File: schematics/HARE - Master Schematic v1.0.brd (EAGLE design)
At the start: 105.1 x 80 mm, 97 parts, among them IC1 NE5532N, IC2 NE5532N, IC3 FT232RL, IC4 NE5532N, IC5 7805DT, IC6 AT25P, J1 9V, J2 STEREOSW, J3 STEREOSW, Q1 16 MHz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

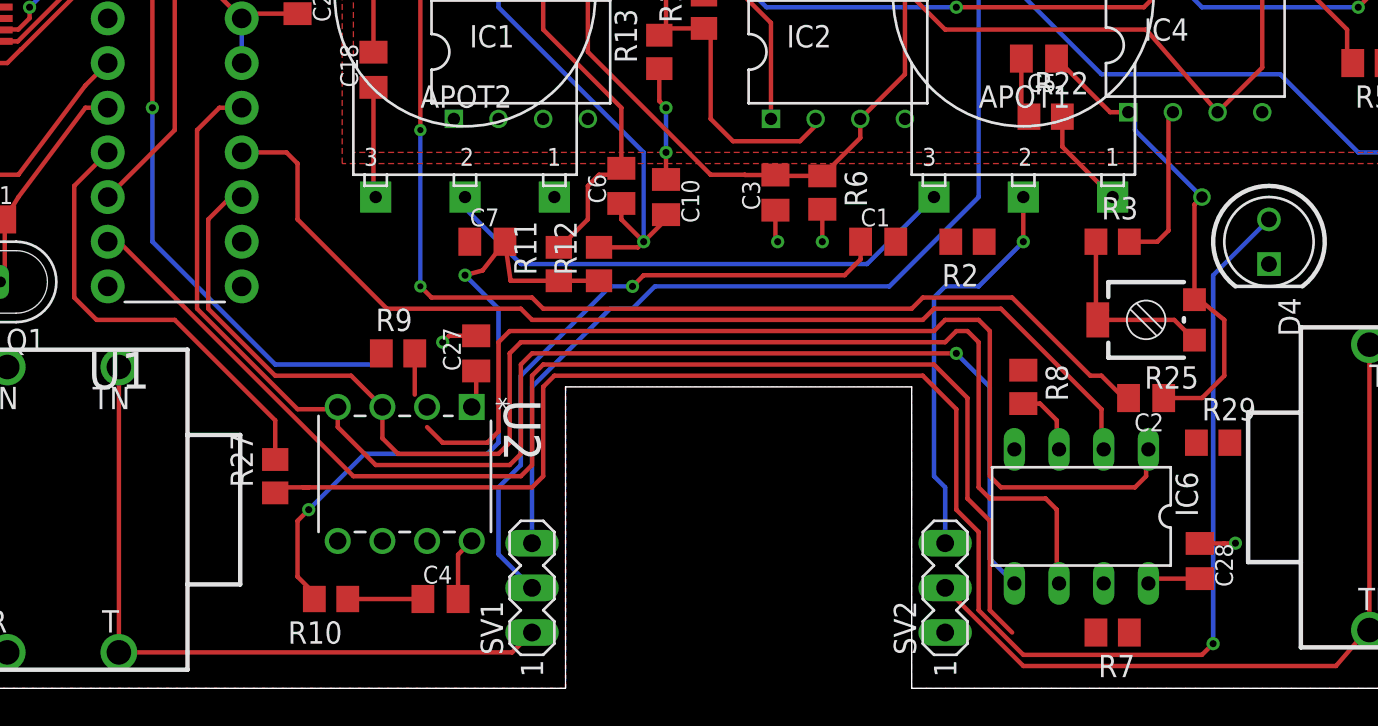
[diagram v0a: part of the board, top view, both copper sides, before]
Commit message: no DRC errors in board file
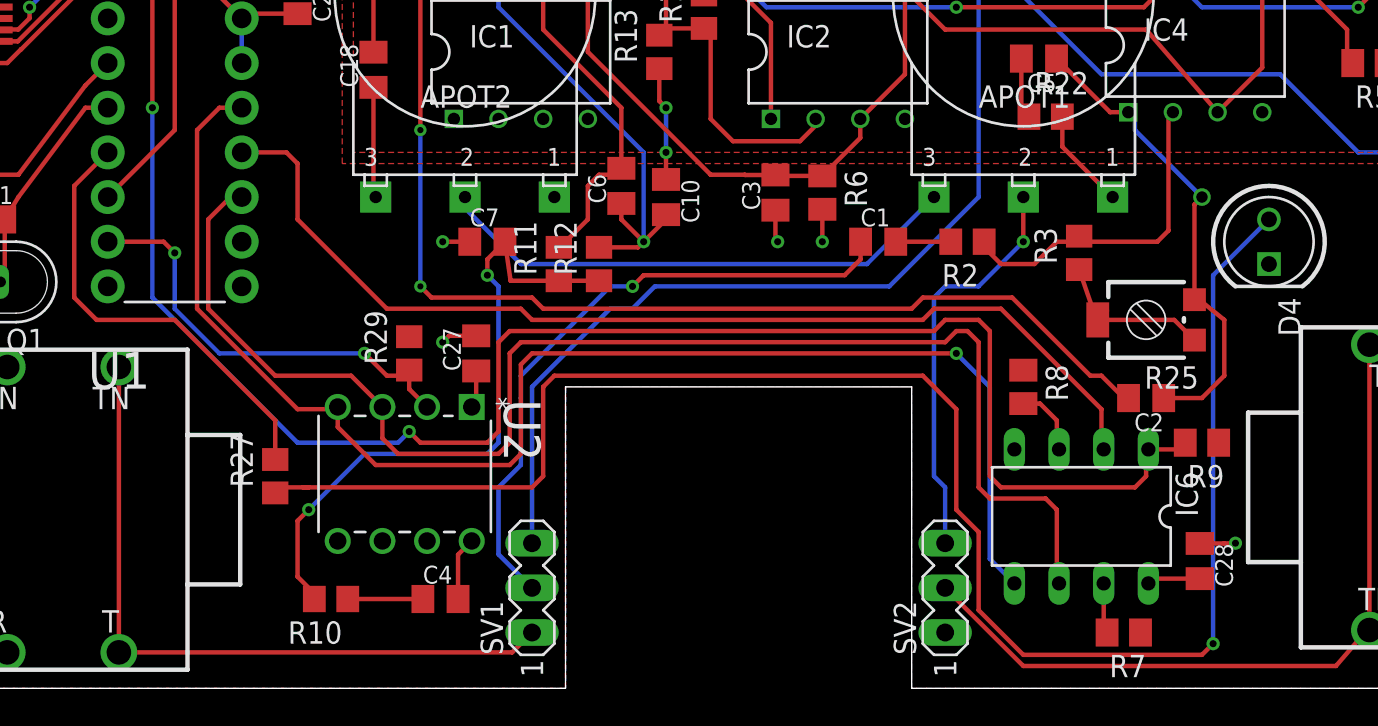
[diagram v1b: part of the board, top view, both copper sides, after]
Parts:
- moved R29 46.0 mm to (33.7, 19.1), turned to 90 degrees
- moved R9 46.0 mm to (78.7, 14.0), turned to 180 degrees
- moved R3 2.01 mm to (71.8, 24.8), turned to 90 degrees
- moved R7 0.64 mm to (74.3, 3.17)
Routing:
- net DAC_CS: track 75.2 -> 25.4 mm, vias 0 -> 2
- net N$11: track 9.32 -> 19.1 mm
- net MEM_CS: track 95.8 -> 102.0 mm, vias 1 -> 2
- net N$10: track 0.00 -> 3.13 mm
- net N$8: track 0.00 -> 2.83 mm
- net GND: track 62.4 -> 63.9 mm, vias 24 -> 25
- net N$49: track 11.4 -> 9.99 mm
- net N$16: track 38.8 -> 37.5 mm

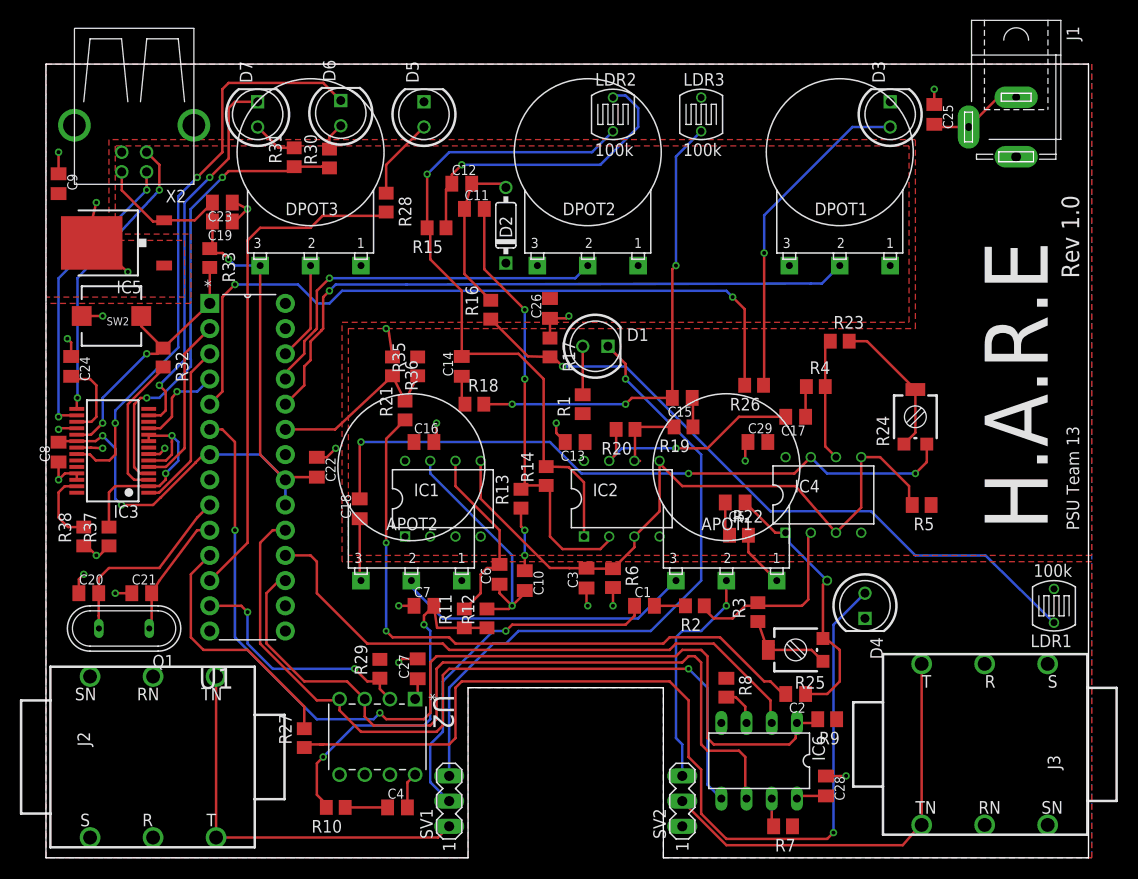
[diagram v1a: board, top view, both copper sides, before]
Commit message: PWM-to-DC converter added for VCA control, VCF changes fixed, and fuse added
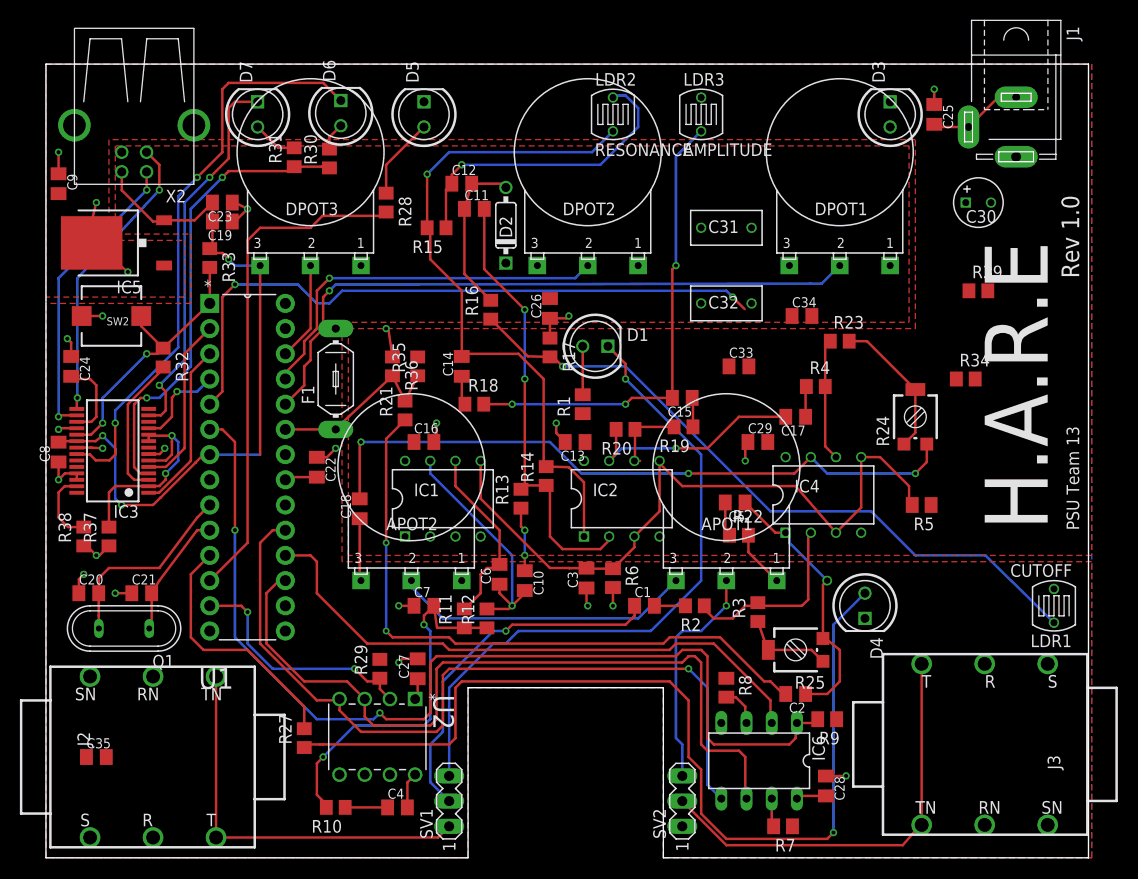
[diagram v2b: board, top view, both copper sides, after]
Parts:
- removed R26: 1k, resistor:R0805
- added C30: 22uF, gm-caps-electro-pol:050_020_1
- added C31, C32: 470nF, gm-caps-film-box:072X035
- added C33, C34: 0.1uF, resistor:C0805K
- added C35: .1uF, resistor:C0805K
- added F1: FUSELITTLEFUSE, fuse:LITTLEFUSE
- added R34, R39: 1k, resistor:R0805
- D3: value LED5MM -> AMPLITUDE
- D4: value LED5MM -> CUTOFF
- D5: value LED5MM -> RESONANCE
- LDR1: value 100k -> CUTOFF
- LDR2: value 100k -> RESONANCE
- LDR3: value 100k -> AMPLITUDE
- R27: value 2.2k -> 1k
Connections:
- removed net N$60: R26.2, U1.5
- removed net N$61: D3.A, R26.1
- new net +5V1: C33.2, U1.21
- new net N$15: C30.+, IC1.2, R34.2, R39.1
- new net N$19: D3.A, IC1.1, R39.2
- new net N$34: C9.2, F1.2, IC5.1
- new net PWM_DC: R34.1, U1.5
- net +5V: now also C16.1, C34.2, IC1.8; no longer U1.21
- net GND: now also C30.-, C31.2, C32.2, C33.1, C34.1, C35.1
- net N$57: now also C31.1
- net N$59: now also C32.1
- net VCC: now also F1.1; no longer C16.1, C9.2, IC1.8, IC5.1
- net V_BIAS: now also C35.2, IC1.3
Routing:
- net N$60: track 74.3 -> 0.00 mm, vias 2 -> 0
- net PWM_DC: track 0.00 -> 66.6 mm, vias 0 -> 2
- net N$61: track 33.6 -> 0.00 mm, vias 1 -> 0
- net +5V: track 89.4 -> 79.3 mm

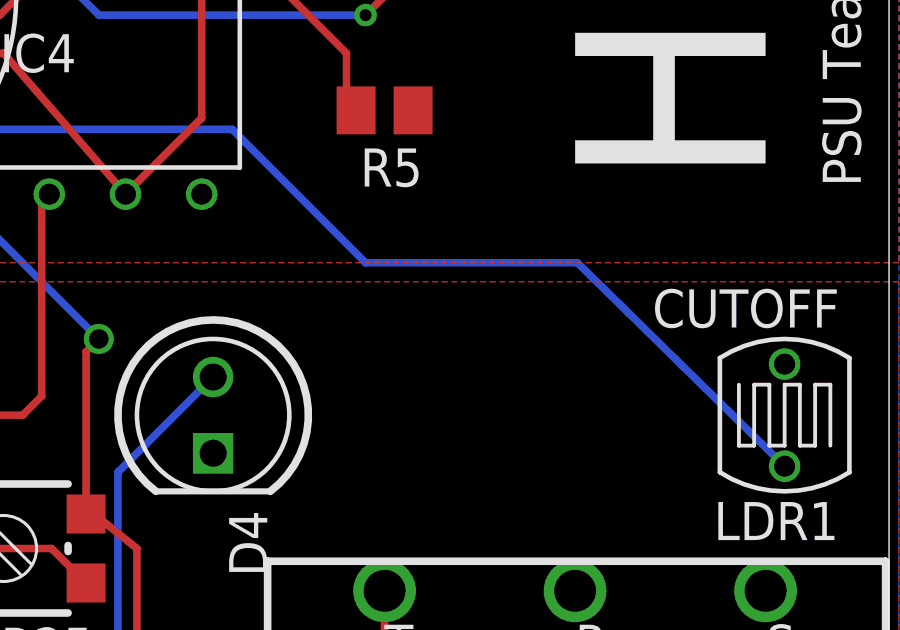
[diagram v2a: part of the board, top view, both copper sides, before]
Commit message: Added filtering cap to analog output circuitry
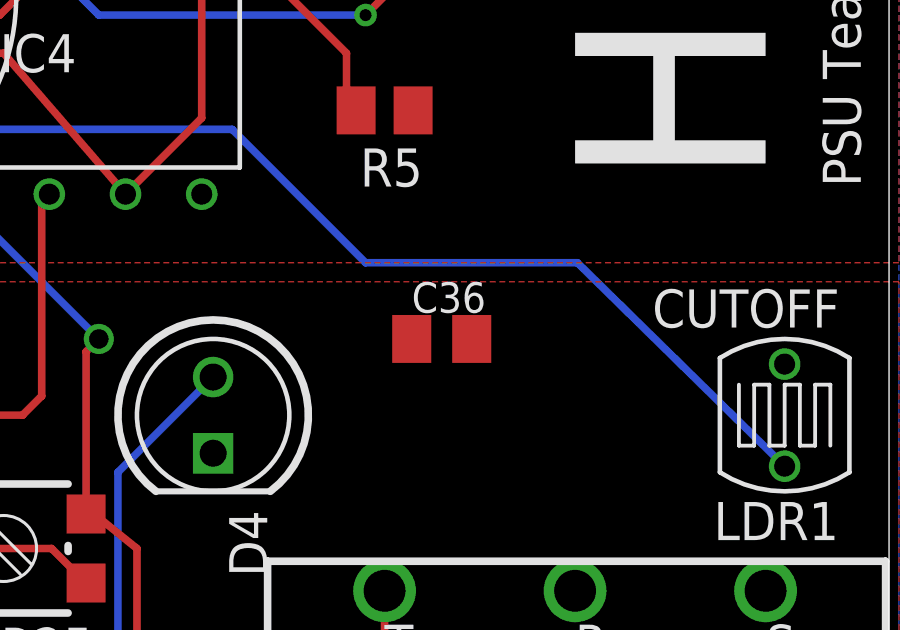
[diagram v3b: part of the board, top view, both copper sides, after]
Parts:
- added C36: 10nF, resistor:C0805K
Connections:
- net N$33: now also C36.2
- net VCA_OUT: now also C36.1
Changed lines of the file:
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@@
 <attribute name="OC_NEWARK" value="unknown" x="29.21" y="48.26" size="1.778" layer="27" rot="R90" display="off"/>
 </element>
+<element name="C36" library="resistor" library_urn="urn:adsk.eagle:library:348" package="C0805K" package3d_urn="urn:adsk.eagle:package:26201/1" value="10nF" x="90.17" y="27.94"/>
 </elements>
 <signals>
@@
 <wire x1="63.312" y1="43.434" x2="59.624" y2="43.434" width="0.254" layer="1"/>
 <wire x1="59.624" y1="43.434" x2="59.37" y2="43.18" width="0.254" layer="1"/>
+<contactref element="C36" pad="2"/>
+<wire x1="91.17" y1="27.94" x2="59.309" y2="40.005" width="0" layer="19" extent="1-1"/>
 </signal>
 <signal name="VCA_OUT">
@@
 <wire x1="58.039" y1="41.275" x2="56.769" y2="40.005" width="0.254" layer="16"/>
 <wire x1="74.565" y1="44.45" x2="69.85" y2="44.45" width="0.254" layer="1"/>
+<contactref element="C36" pad="1"/>
+<wire x1="89.17" y1="27.94" x2="56.769" y2="40.005" width="0" layer="19" extent="1-1"/>
 </signal>
 <signal name="ADC_IN">

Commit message: Added high frequency filter cap to analog output circuitry
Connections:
- net N$33: no longer C36.2
- net N$41: now also C36.2
- net N$43: now also C36.1
- net VCA_OUT: no longer C36.1
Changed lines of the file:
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@@
 <wire x1="63.312" y1="43.434" x2="59.624" y2="43.434" width="0.254" layer="1"/>
 <wire x1="59.624" y1="43.434" x2="59.37" y2="43.18" width="0.254" layer="1"/>
-<contactref element="C36" pad="2"/>
-<wire x1="91.17" y1="27.94" x2="59.309" y2="40.005" width="0" layer="19" extent="1-1"/>
 </signal>
 <signal name="VCA_OUT">
@@
 <wire x1="58.039" y1="41.275" x2="56.769" y2="40.005" width="0.254" layer="16"/>
 <wire x1="74.565" y1="44.45" x2="69.85" y2="44.45" width="0.254" layer="1"/>
-<contactref element="C36" pad="1"/>
-<wire x1="89.17" y1="27.94" x2="56.769" y2="40.005" width="0" layer="19" extent="1-1"/>
 </signal>
 <signal name="ADC_IN">
@@
 <wire x1="78.547" y1="47.498" x2="78.547" y2="51.557" width="0.254" layer="1"/>
 <wire x1="78.547" y1="51.557" x2="79.06" y2="52.07" width="0.254" layer="1"/>
+<contactref element="C36" pad="2"/>
+<wire x1="91.17" y1="27.94" x2="79.629" y2="40.386" width="0" layer="19" extent="1-1"/>
 </signal>
 <signal name="N$42">
@@
 <wire x1="64.77" y1="38.735" x2="75.438" y2="38.735" width="0.254" layer="1"/>
 <wire x1="75.438" y1="38.735" x2="77.089" y2="40.386" width="0.254" layer="1"/>
+<contactref element="C36" pad="1"/>
+<wire x1="87.63" y1="38.735" x2="89.17" y2="27.94" width="0" layer="19" extent="1-1"/>
 </signal>
 <signal name="N$45">

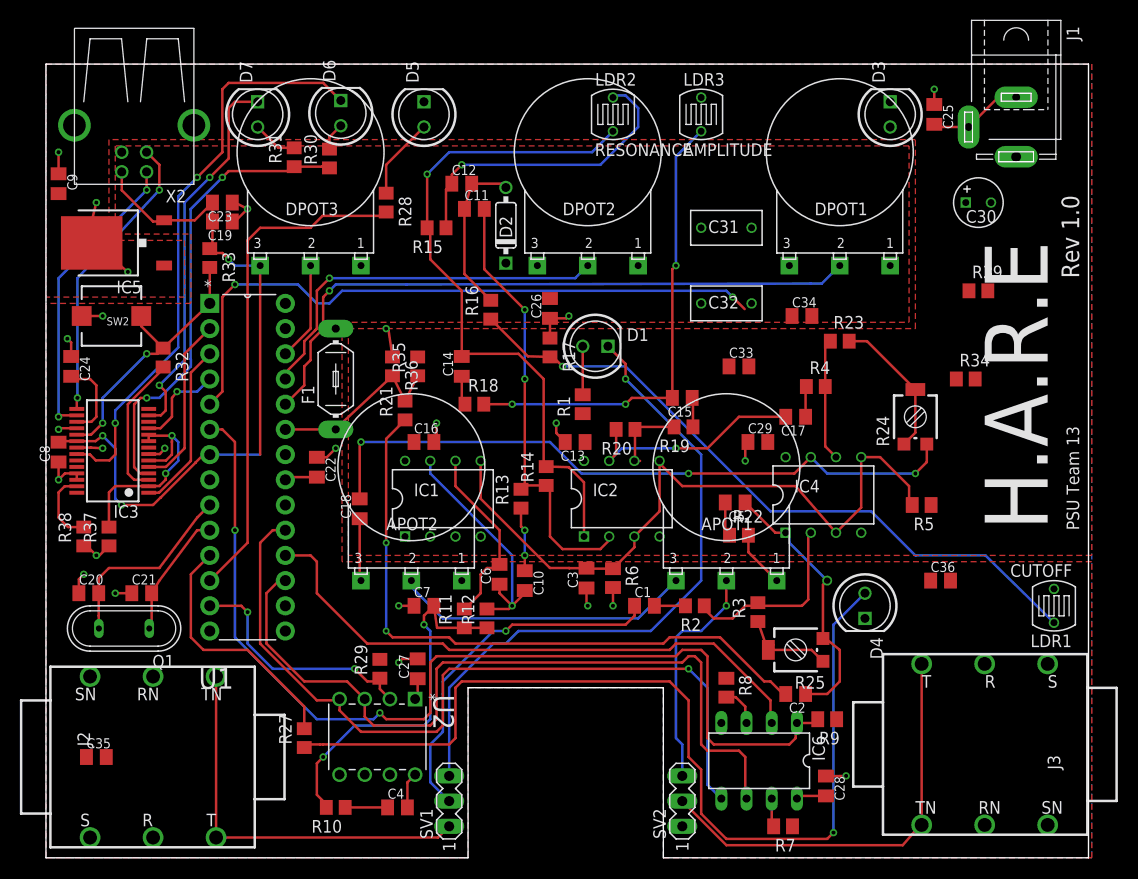
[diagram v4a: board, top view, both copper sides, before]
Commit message: Completed routing high frequency filter caps
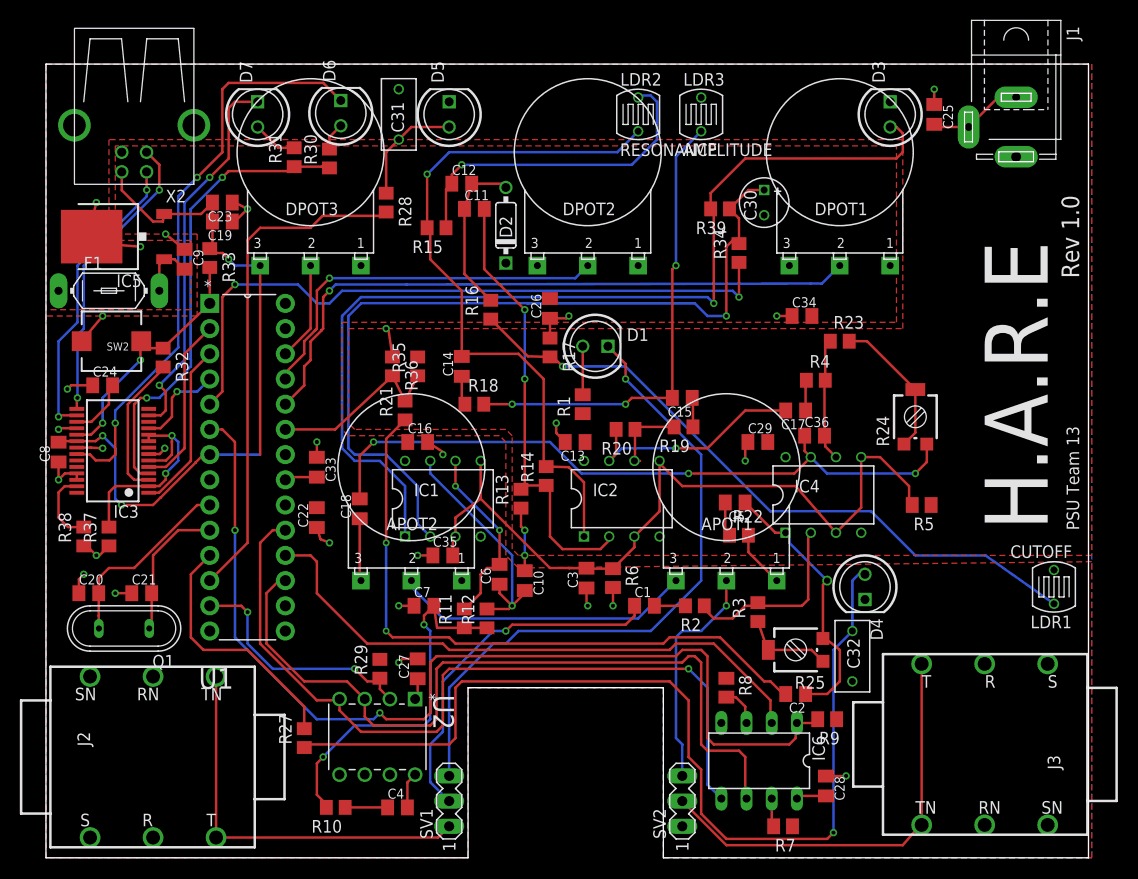
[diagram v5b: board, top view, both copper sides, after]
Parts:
- moved C33 43.7 mm to (27.3, 39.4), turned to 270 degrees
- moved C35 40.4 mm to (40.0, 30.5)
- moved C32 37.8 mm to (81.3, 20.3), turned to 270 degrees
- moved C31 34.9 mm to (35.6, 74.9), turned to 90 degrees
- moved R39 27.3 mm to (67.9, 65.4), turned to 180 degrees
- moved R34 26.2 mm to (69.8, 61.0), turned to 90 degrees
- moved F1 24.5 mm to (6.35, 57.1), turned to 0 degrees
- moved C30 21.6 mm to (72.4, 66.0), turned to 270 degrees
- moved C36 19.4 mm to (77.5, 42.5)
- moved C9 14.8 mm to (14.0, 60.3)
- moved C22 5.08 mm to (27.3, 34.3), turned to 90 degrees
- moved C24 3.70 mm to (5.71, 47.6), turned to 0 degrees
- moved D5 2.54 mm to (40.6, 74.9)
- moved LDR2 2.54 mm to (59.7, 74.9)
- moved SW2 2.54 mm to (6.60, 52.1)
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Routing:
- net N$19: track 0.00 -> 100.6 mm, vias 0 -> 1
- net N$15: track 0.00 -> 83.5 mm, vias 0 -> 1
- net GND: track 63.9 -> 71.8 mm, vias 25 -> 28
- net V_BIAS: track 70.9 -> 78.0 mm
- net N$34: track 0.00 -> 5.86 mm
- net +5V1: track 0.00 -> 3.29 mm
- net N$57: track 8.25 -> 11.5 mm
- net +5V: track 79.3 -> 76.7 mm
- net VCA_IN: track 68.6 -> 71.1 mm
- net RESET#: track 28.1 -> 25.6 mm
- net PWM_DC: track 66.6 -> 69.0 mm
- net N$25: track 31.4 -> 33.8 mm
- net N$59: track 97.3 -> 99.6 mm
- net N$54: track 8.27 -> 6.04 mm
- net N$43: track 67.8 -> 69.5 mm
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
